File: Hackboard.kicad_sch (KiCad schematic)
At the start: 48 parts, among them J1 Barrel_Jack, J2 USB_C_Receptacle_USB2.0_16P, J3 Micro_SD_Card, J4 Conn_01x31_Socket, J5 Conn_01x31_Socket, SW1 SW_MEC_5E, U1 STM32L476RGT6, U2 AP63205WU, U3 NCP164CSN330T1G, U4 USBLC6-2SC6

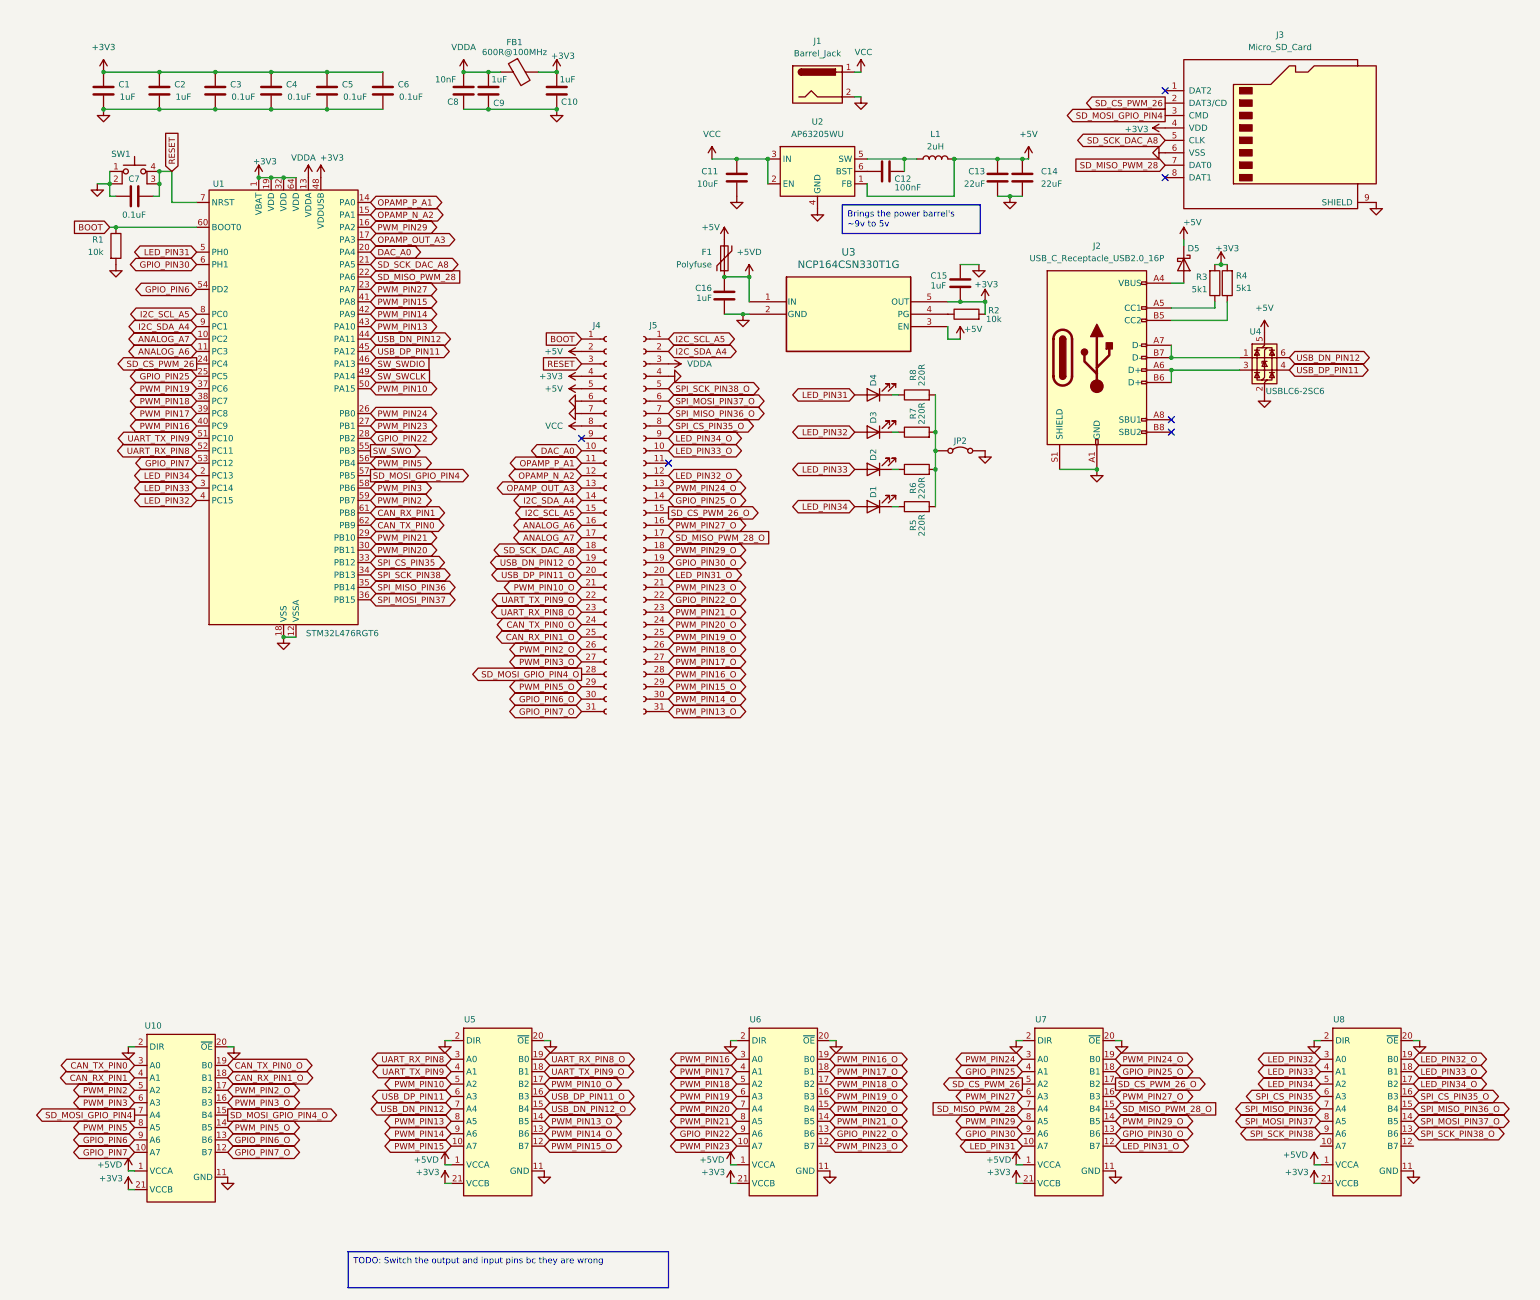
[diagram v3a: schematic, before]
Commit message: Finish schematic
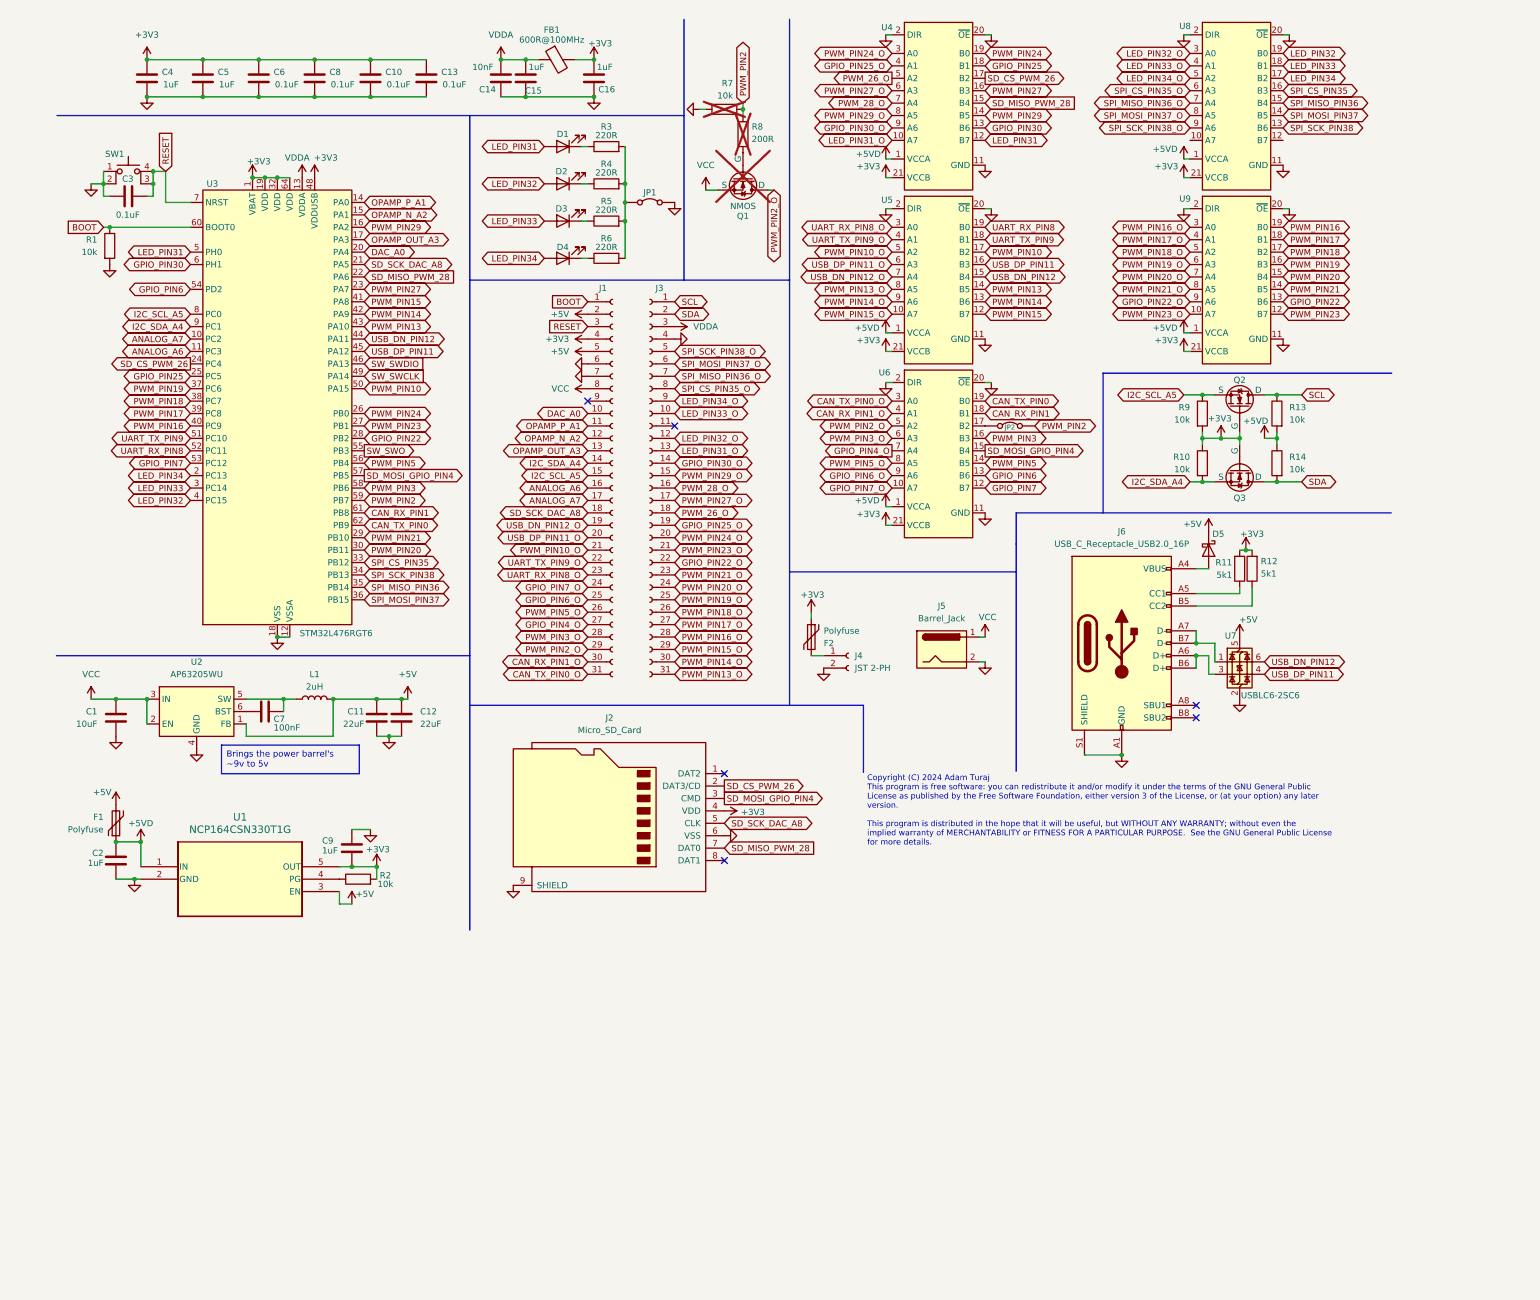
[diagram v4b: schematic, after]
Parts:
- added F2: Polyfuse, symbol Device:Polyfuse
- added J4: JST 2-PH, symbol Connector:Conn_01x02_Socket
- added JP2: Jumper_2_Bridged, symbol Jumper:Jumper_2_Bridged
- added Q1, Q2, Q3: NMOS, symbol Simulation_SPICE:NMOS
- added R10, R13, R14, R7, R9: 10k, symbol Device:R
- added R8: 200R, symbol Device:R
- renumbered C11 to C1, C5 to C10, C13 to C11, C14 to C12, C6 to C13, C8 to C14, C9 to C15, C10 to C16, C16 to C2, C7 to C3, C1 to C4, C2 to C5, C3 to C6, C12 to C7, C4 to C8, C15 to C9, D4 to D1, D3 to D2, D2 to D3, D1 to D4, J4 to J1, J3 to J2, J5 to J3, J1 to J5, J2 to J6, JP2 to JP1, R3 to R11, R4 to R12, R8 to R3, R7 to R4, R6 to R5, R5 to R6, U3 to U1, U1 to U3, U7 to U4, U10 to U6, U4 to U7, U6 to U9
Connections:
- net +3V3: now also F2.1, Q2.2 (G), Q3.2 (G), R10.1, R9.2
- net +5VD: now also R13.2, R14.1
- net CAN_RX_PIN1: now also U6.18 (B1); no longer U6.4 (A1)
- net CAN_RX_PIN1_O: now also J1.30 (Pin_30), U6.4 (A1); no longer J1.25 (Pin_25), U6.18 (B1)
- net CAN_TX_PIN0: now also U6.19 (B0); no longer U6.3 (A0)
- net CAN_TX_PIN0_O: now also J1.31 (Pin_31), U6.3 (A0); no longer J1.24 (Pin_24), U6.19 (B0)
- net GND: now also J4.2 (Pin_2), R7.2
- net GPIO_PIN22: now also U9.13 (B6); no longer U9.9 (A6)
- net GPIO_PIN22_O: now also J3.22 (Pin_22), U9.9 (A6); no longer U9.13 (B6)
- net GPIO_PIN25: now also U4.18 (B1); no longer U4.4 (A1)
- net GPIO_PIN25_O: now also J3.19 (Pin_19), U4.4 (A1); no longer J3.14 (Pin_14), U4.18 (B1)
- net GPIO_PIN30: now also U4.13 (B6); no longer U4.9 (A6)
- net GPIO_PIN30_O: now also J3.14 (Pin_14), U4.9 (A6); no longer J3.19 (Pin_19), U4.13 (B6)
- net GPIO_PIN6: now also U6.13 (B6); no longer U6.9 (A6)
- net GPIO_PIN6_O: now also J1.25 (Pin_25), U6.9 (A6); no longer J1.30 (Pin_30), U6.13 (B6)
- net GPIO_PIN7: now also U6.12 (B7); no longer U6.10 (A7)
- net GPIO_PIN7_O: now also J1.24 (Pin_24), U6.10 (A7); no longer J1.31 (Pin_31), U6.12 (B7)
- net I2C_SCL_A5: now also Q2.3 (S), R9.1; no longer J3.1 (Pin_1)
- net I2C_SDA_A4: now also Q3.3 (S), R10.2; no longer J3.2 (Pin_2)
- net LED_PIN31: now also U4.12 (B7); no longer U4.10 (A7)
- net LED_PIN31_O: now also J3.13 (Pin_13), U4.10 (A7); no longer J3.20 (Pin_20), U4.12 (B7)
- net LED_PIN32: now also U8.19 (B0); no longer U8.3 (A0)
- net LED_PIN32_O: now also U8.3 (A0); no longer U8.19 (B0)
- net LED_PIN33: now also U8.18 (B1); no longer U8.4 (A1)
- net LED_PIN33_O: now also U8.4 (A1); no longer U8.18 (B1)
- net LED_PIN34: now also U8.17 (B2); no longer U8.5 (A2)
- net LED_PIN34_O: now also U8.5 (A2); no longer U8.17 (B2)
- net PWM_PIN10: now also U5.17 (B2); no longer U5.5 (A2)
- net PWM_PIN10_O: now also U5.5 (A2); no longer U5.17 (B2)
- net PWM_PIN13: now also U5.14 (B5); no longer U5.8 (A5)
- net PWM_PIN13_O: now also U5.8 (A5); no longer U5.14 (B5)
- net PWM_PIN14: now also U5.13 (B6); no longer U5.9 (A6)
- net PWM_PIN14_O: now also U5.9 (A6); no longer U5.13 (B6)
- net PWM_PIN15: now also U5.12 (B7); no longer U5.10 (A7)
- net PWM_PIN15_O: now also U5.10 (A7); no longer U5.12 (B7)
- net PWM_PIN16: now also U9.19 (B0); no longer U9.3 (A0)
- net PWM_PIN16_O: now also J3.28 (Pin_28), U9.3 (A0); no longer U9.19 (B0)
- net PWM_PIN17: now also U9.18 (B1); no longer U9.4 (A1)
- net PWM_PIN17_O: now also J3.27 (Pin_27), U9.4 (A1); no longer U9.18 (B1)
- net PWM_PIN18: now also U9.17 (B2); no longer U9.5 (A2)
- net PWM_PIN18_O: now also J3.26 (Pin_26), U9.5 (A2); no longer U9.17 (B2)
- net PWM_PIN19: now also U9.16 (B3); no longer U9.6 (A3)
- net PWM_PIN19_O: now also J3.25 (Pin_25), U9.6 (A3); no longer U9.16 (B3)
- net PWM_PIN2: now also JP2.1 (A), R7.1, R8.2; no longer U6.5 (A2)
- net PWM_PIN20: now also U9.15 (B4); no longer U9.7 (A4)
- net PWM_PIN20_O: now also J3.24 (Pin_24), U9.7 (A4); no longer U9.15 (B4)
- net PWM_PIN21: now also U9.14 (B5); no longer U9.8 (A5)
- net PWM_PIN21_O: now also J3.23 (Pin_23), U9.8 (A5); no longer U9.14 (B5)
- net PWM_PIN23: now also U9.12 (B7); no longer U9.10 (A7)
- net PWM_PIN23_O: now also J3.21 (Pin_21), U9.10 (A7); no longer U9.12 (B7)
- net PWM_PIN24: now also U4.19 (B0); no longer U4.3 (A0)
- net PWM_PIN24_O: now also J3.20 (Pin_20), U4.3 (A0); no longer J3.13 (Pin_13), U4.19 (B0)
- net PWM_PIN27: now also U4.16 (B3); no longer U4.6 (A3)
- net PWM_PIN27_O: now also J3.17 (Pin_17), U4.6 (A3); no longer J3.16 (Pin_16), U4.16 (B3)
- net PWM_PIN29: now also U4.14 (B5); no longer U4.8 (A5)
- net PWM_PIN29_O: now also J3.15 (Pin_15), U4.8 (A5); no longer J3.18 (Pin_18), U4.14 (B5)
- net PWM_PIN2_O: now also J1.29 (Pin_29), U6.5 (A2), Q1.1 (D); no longer J1.26 (Pin_26), U6.17 (B2)
- net PWM_PIN3: now also U6.16 (B3); no longer U6.6 (A3)
- net PWM_PIN3_O: now also J1.28 (Pin_28), U6.6 (A3); no longer J1.27 (Pin_27), U6.16 (B3)
- net PWM_PIN5: now also U6.14 (B5); no longer U6.8 (A5)
- net PWM_PIN5_O: now also J1.26 (Pin_26), U6.8 (A5); no longer J1.29 (Pin_29), U6.14 (B5)
- net SD_CS_PWM_26: now also U4.17 (B2); no longer U4.5 (A2)
- net SD_MISO_PWM_28: now also U4.15 (B4); no longer U4.7 (A4)
- net SD_MOSI_GPIO_PIN4: now also U6.15 (B4); no longer U6.7 (A4)
- net SPI_CS_PIN35: now also U8.16 (B3); no longer U8.6 (A3)
- net SPI_CS_PIN35_O: now also U8.6 (A3); no longer U8.16 (B3)
- net SPI_MISO_PIN36: now also U8.15 (B4); no longer U8.7 (A4)
- net SPI_MISO_PIN36_O: now also U8.7 (A4); no longer U8.15 (B4)
- net SPI_MOSI_PIN37: now also U8.14 (B5); no longer U8.8 (A5)
- net SPI_MOSI_PIN37_O: now also U8.8 (A5); no longer U8.14 (B5)
- net SPI_SCK_PIN38: now also U8.13 (B6); no longer U8.9 (A6)
- net SPI_SCK_PIN38_O: now also U8.9 (A6); no longer U8.13 (B6)
- net UART_RX_PIN8: now also U5.19 (B0); no longer U5.3 (A0)
- net UART_RX_PIN8_O: now also U5.3 (A0); no longer U5.19 (B0)
- net UART_TX_PIN9: now also U5.18 (B1); no longer U5.4 (A1)
- net UART_TX_PIN9_O: now also U5.4 (A1); no longer U5.18 (B1)
- net USB_DN_PIN12: now also U5.15 (B4); no longer U5.7 (A4)
- net USB_DN_PIN12_O: now also U5.7 (A4); no longer U5.15 (B4)
- net USB_DP_PIN11: now also U5.16 (B3); no longer U5.6 (A3)
- net USB_DP_PIN11_O: now also U5.6 (A3); no longer U5.16 (B3)
- net VCC: now also Q1.3 (S)
- removed net SD_CS_PWM_26_O: J3.15 (Pin_15), U4.17 (B2)
- removed net SD_MISO_PWM_28_O: J3.17 (Pin_17), U4.15 (B4)
- removed net SD_MOSI_GPIO_PIN4_O: J1.28 (Pin_28), U6.15 (B4)
- new net: JP2.2 (B), U6.17 (B2)
- new net: F2.2, J4.1 (Pin_1)
- new net: Q1.2 (G), R8.1
- new net GPIO_PIN4_O: J1.27 (Pin_27), U6.7 (A4)
- new net PWM_26_O: J3.18 (Pin_18), U4.5 (A2)
- new net PWM_28_O: J3.16 (Pin_16), U4.7 (A4)
- new net SCL: J3.1 (Pin_1), Q2.1 (D), R13.1
- new net SDA: J3.2 (Pin_2), Q3.1 (D), R14.2
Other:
- note added: "Copyright (C) 2024 Adam Turaj This program is free software: you can redistribute it and/or modify it under the terms of the GNU General Public License as published by the Free Software Foundation, either version 3 of the License, or (at your option) any later version. This program is distributed in the hope that it will be useful, but WITHOUT ANY WARRANTY; without even the implied warranty of ME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"
- title: (none) -> Hackboard
- moved on the sheet: C1, C10, C11, C12, C13, C14, C15, C16, C2, C3, C4, C5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

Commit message: Make changes to schematic and start adding footprints
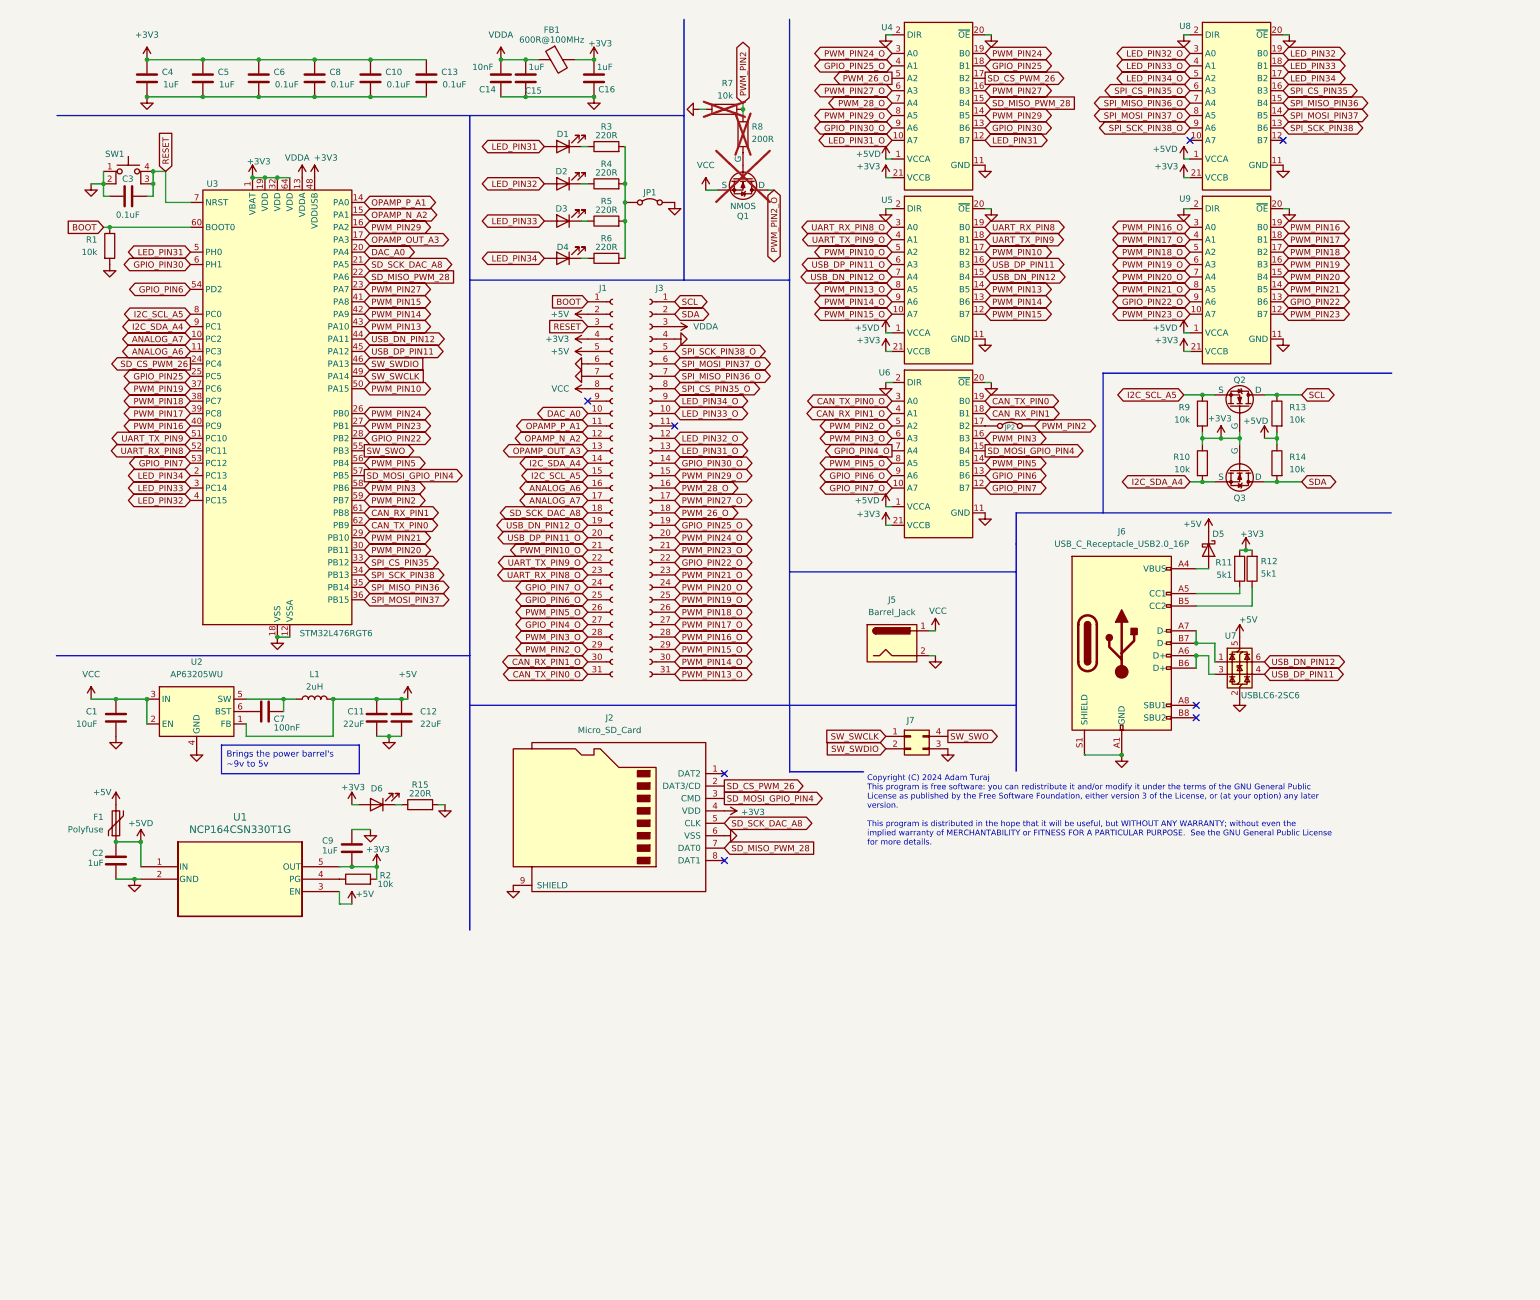
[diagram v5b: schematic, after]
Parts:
- removed F2: Polyfuse, symbol Device:Polyfuse
- removed J4: JST 2-PH, symbol Connector:Conn_01x02_Socket
- added D6: LED, LED_SMD:LED_0603_1608Metric, symbol Device:LED
- added J7: Conn_02x02_Counter_Clockwise, symbol Connector_Generic:Conn_02x02_Counter_Clockwise
- added R15: 220R, Resistor_SMD:R_0603_1608Metric, symbol Device:R
- C1, C10, C11, C12, C13, C14, C15, C16, C2, C3, C4, C5, C6, C7, C8, C9: footprint (none) -> Capacitor_SMD:C_0603_1608Metric
- D1, D2, D3, D4: footprint (none) -> LED_SMD:LED_0603_1608Metric
- D5: footprint (none) -> DO-221AC:VSSAF3L63HM3
- L1: footprint (none) -> Inductor_SMD:L_Vishay_IFSC-1515AH_4x4x1.8mm
- R1, R10, R11, R12, R13, R14, R2, R3, R4, R5, R6, R7, R8, R9: footprint (none) -> Resistor_SMD:R_0603_1608Metric
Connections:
- net +3V3: now also D6.2 (A)
- net GND: now also J7.3 (Pin_3), R15.2
- net SW_SWCLK: now also J7.1 (Pin_1)
- net SW_SWDIO: now also J7.2 (Pin_2)
- net SW_SWO: now also J7.4 (Pin_4)
- new net: D6.1 (K), R15.1
- no-connect marks 6 -> 8
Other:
- moved on the sheet: J5
